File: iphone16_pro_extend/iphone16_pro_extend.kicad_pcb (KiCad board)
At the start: 4 copper layers, 89.8 x 97.4 mm, 20 parts, among them CN1 20455-020E-02, CN2 20455-020E-02, CN3 20455-020E-02, CN4 20455-020E-02, J3 Conn_01x20_Pin, J4 Conn_01x04_Pin, J5 Conn_01x20_Pin, J6 Conn_01x04_Pin

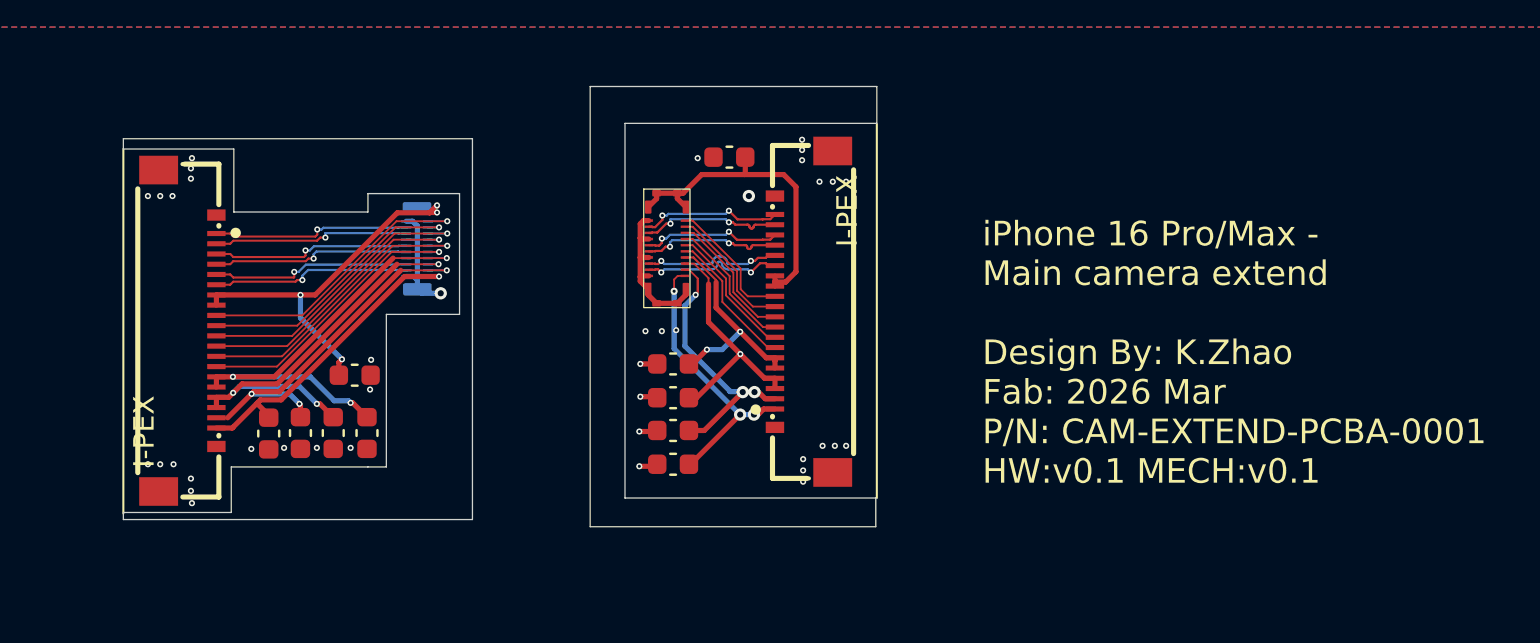
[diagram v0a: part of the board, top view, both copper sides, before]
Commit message: Change via diameter to 0.3/0.4mm, reroute
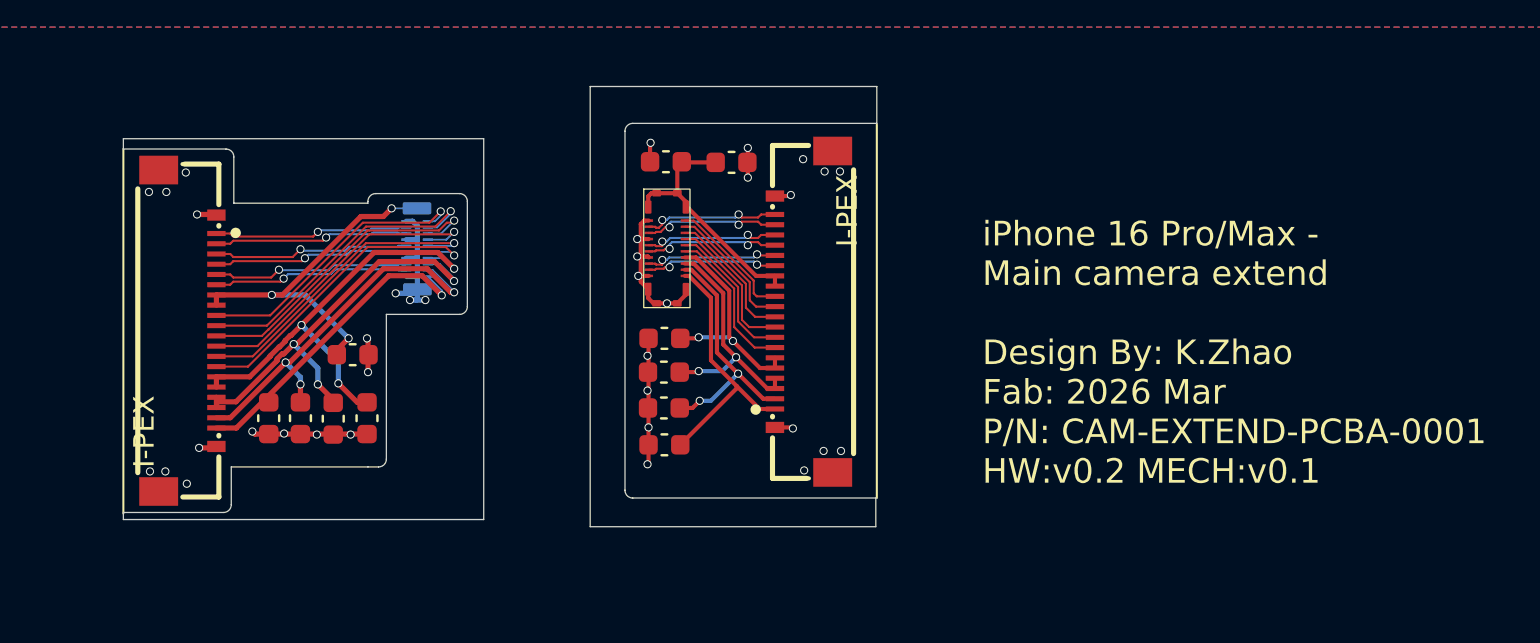
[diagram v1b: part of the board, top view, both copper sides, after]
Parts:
- added C11: 100n, Capacitor_SMD:C_0603_1608Metric, F.Cu at (65.1, 54.2)
- moved C1 3.11 mm to (61.9, 54.1)
- moved C3 1.33 mm to (61.8, 64.4)
- moved C2 1.32 mm to (61.8, 62.8)
- moved C4 1.19 mm to (61.8, 66.2)
- moved C5 1.04 mm to (61.8, 68.0)
- moved C10 1.00 mm to (46.6, 63.5)
- moved C9 0.75 mm to (42.5, 66.7)
- moved C6 0.72 mm to (47.3, 66.7)
- moved C8 0.72 mm to (44.0, 66.7)
- moved C7 0.70 mm to (45.6, 66.7)
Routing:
- net GND: track 18.0 -> 35.1 mm, vias 75 -> 72
- net /RECEP_to_20455/POWER_1V47: track 15.9 -> 12.4 mm
- net /PLUG_to_20455/POWER_1V47: track 20.4 -> 17.7 mm, vias 4 -> 3
- net /RECEP_to_20455/POWER_1V8: track 14.4 -> 12.2 mm, vias 3 -> 2
- net /PLUG_to_20455/PMU_SHUTDOWN: track 13.4 -> 15.3 mm
- net /PLUG_to_20455/PMU_SCL: track 13.7 -> 15.6 mm
- net /PLUG_to_20455/STROBE: track 13.6 -> 15.4 mm
- net /PLUG_to_20455/SYNC: track 14.3 -> 15.5 mm
- net /RECEP_to_20455/POWER_VAR: track 14.0 -> 12.9 mm, vias 4 -> 0
- net /RECEP_to_20455/PMU_SDA: track 6.23 -> 7.25 mm
- net /PLUG_to_20455/PMU_SDA: track 14.5 -> 15.2 mm
- net /PLUG_to_20455/POWER_1V8: track 18.4 -> 19.1 mm
- net /PLUG_to_20455/POWER_2V75: track 20.3 -> 21.0 mm
- net /RECEP_to_20455/PMU_SCL: track 6.77 -> 7.45 mm
- net /RECEP_to_20455/STROBE: track 6.51 -> 7.17 mm
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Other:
- outline, holes or cut-outs redrawn
- board text added: "iPhone 16 Pro/Max - Main camera extend Design By: K.Zhao Fab: 2026 Mar P/N: CAM-EXTEND-PCBA-0001 HW:v0.2 MECH:v0.1"
- board text removed: "iPhone 16 Pro/Max - Main camera extend Design By: K.Zhao Fab: 2026 Mar P/N: CAM-EXTEND-PCBA-0001 HW:v0.1 MECH:v0.1"

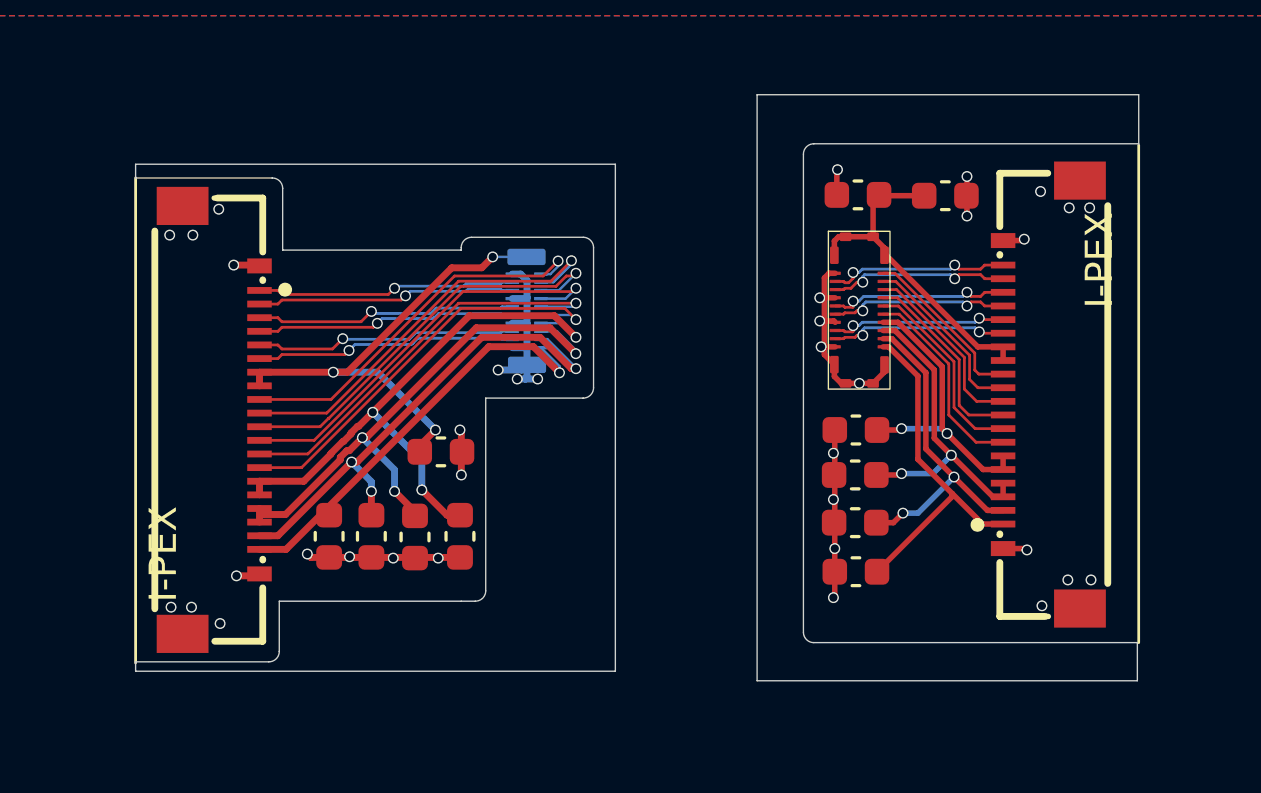
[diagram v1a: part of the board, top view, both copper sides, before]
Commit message: Change via holes to 0.35/0.45
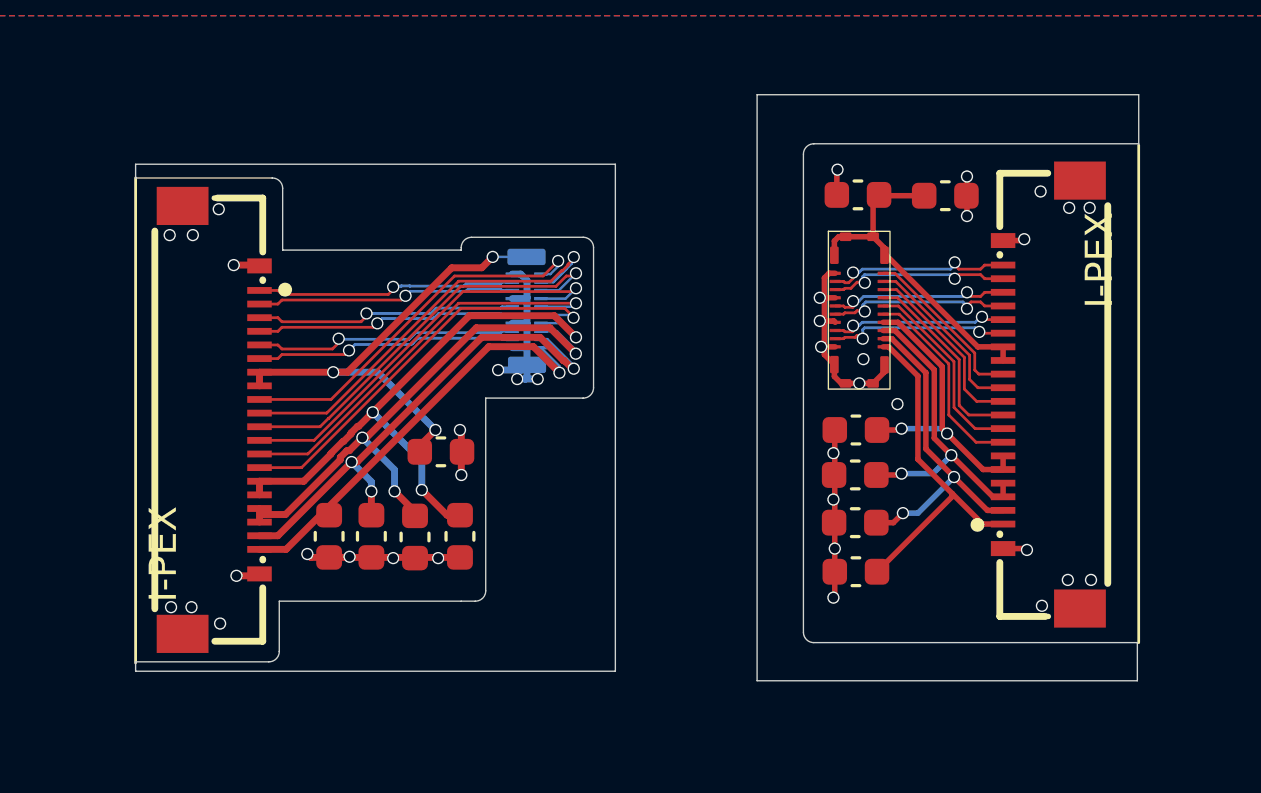
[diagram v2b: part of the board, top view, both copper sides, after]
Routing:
- net GND: vias 72 -> 74
